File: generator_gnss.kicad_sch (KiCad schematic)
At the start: 0 parts

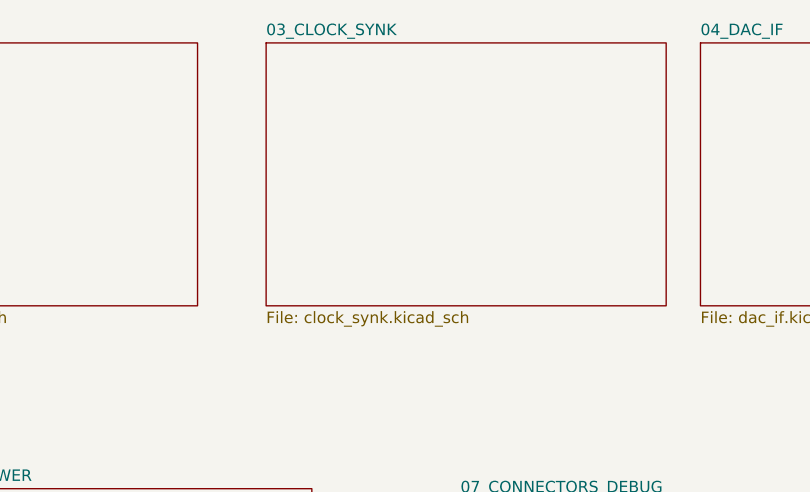
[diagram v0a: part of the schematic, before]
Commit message: Rename schems
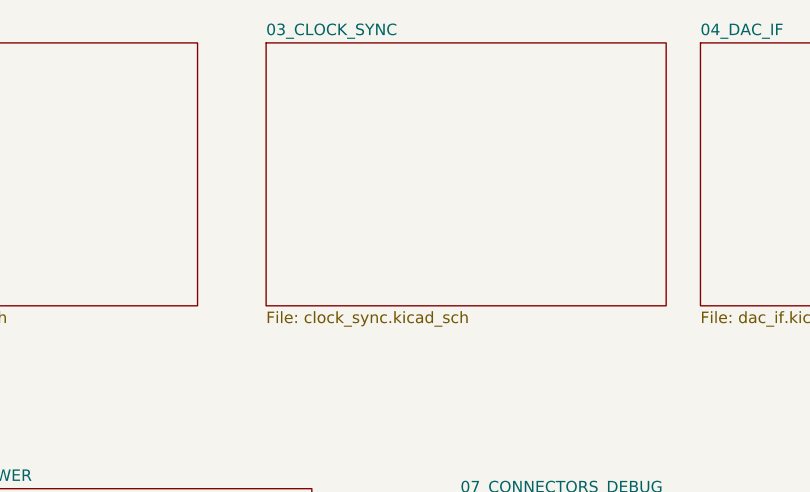
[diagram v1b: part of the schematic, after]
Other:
- sheet 03_CLOCK_SYNK renamed 03_CLOCK_SYNC
- sheet 03_CLOCK_SYNC: file clock_synk.kicad_sch -> clock_sync.kicad_sch
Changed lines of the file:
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@@
 		)
 		(instances
-			(project "immitator_gnns"
+			(project "generator_gnss"
 				(path "/f9f7661c-8604-4706-903b-5ef481cc0e7c"
 					(page "5")
@@
 		)
 		(instances
-			(project "immitator_gnns"
+			(project "generator_gnss"
 				(path "/f9f7661c-8604-4706-903b-5ef481cc0e7c"
 					(page "2")
@@
 		)
 		(instances
-			(project "immitator_gnns"
+			(project "generator_gnss"
 				(path "/f9f7661c-8604-4706-903b-5ef481cc0e7c"
 					(page "8")
@@
 		)
 		(instances
-			(project "immitator_gnns"
+			(project "generator_gnss"
 				(path "/f9f7661c-8604-4706-903b-5ef481cc0e7c"
 					(page "7")
@@
 			(color 0 0 0 0.0000)
 		)
-		(property "Sheetname" "03_CLOCK_SYNK"
+		(property "Sheetname" "03_CLOCK_SYNC"
 			(at 118.11 19.6084 0)
 			(effects
@@
 			)
 		)
-		(property "Sheetfile" "clock_synk.kicad_sch"
+		(property "Sheetfile" "clock_sync.kicad_sch"
 			(at 118.11 50.1146 0)
 			(effects
@@
 		)
 		(instances
-			(project "immitator_gnns"
+			(project "generator_gnss"
 				(path "/f9f7661c-8604-4706-903b-5ef481cc0e7c"
 					(page "4")
@@
 		)
 		(instances
-			(project "immitator_gnns"
+			(project "generator_gnss"
 				(path "/f9f7661c-8604-4706-903b-5ef481cc0e7c"
 					(page "3")
@@
 		)
 		(instances
-			(project "immitator_gnns"
+			(project "generator_gnss"
 				(path "/f9f7661c-8604-4706-903b-5ef481cc0e7c"
 					(page "6")

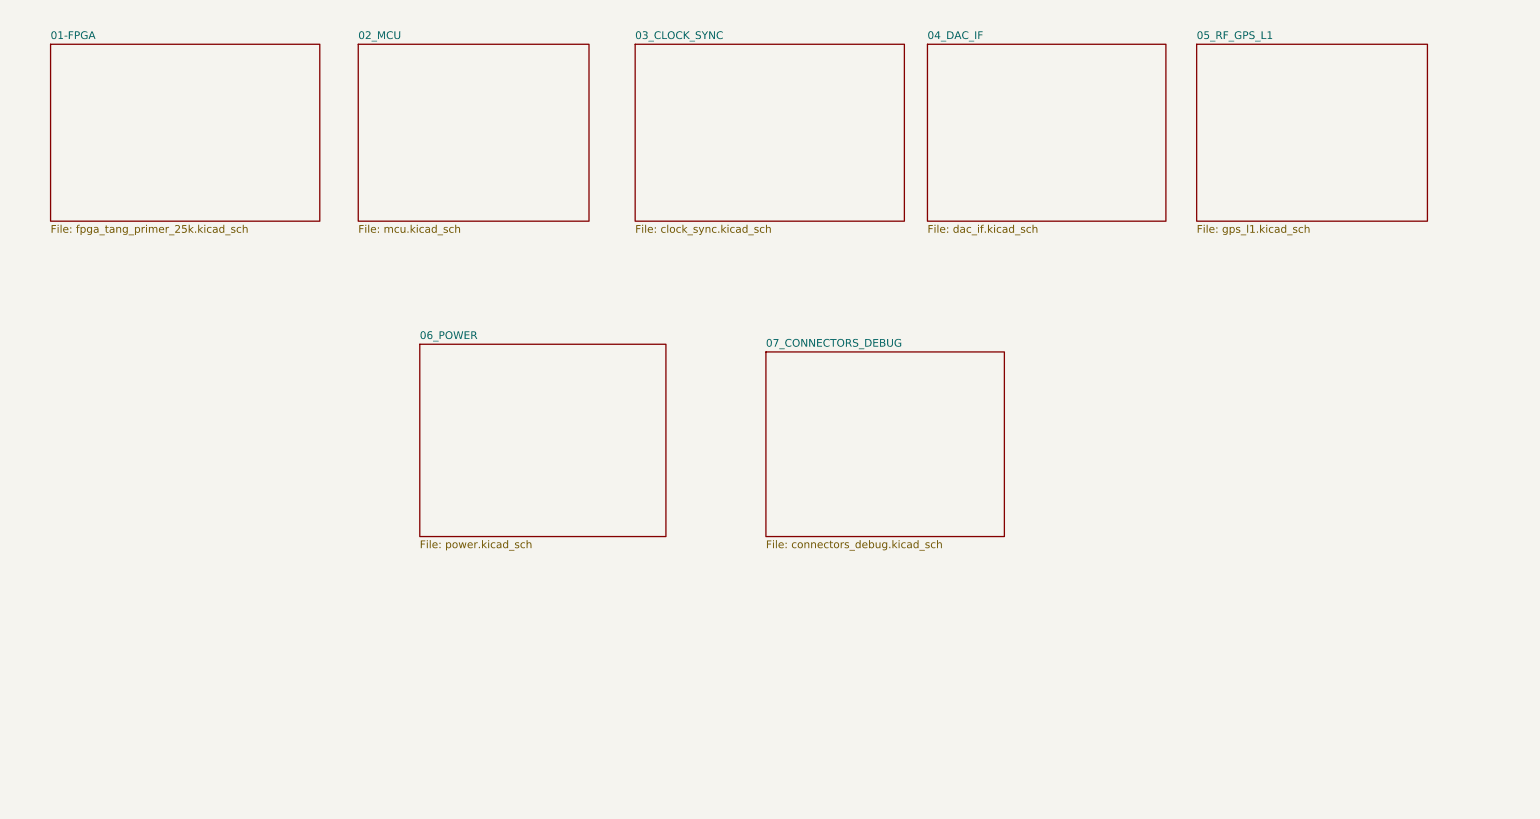
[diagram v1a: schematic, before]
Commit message: Turn to new version Kicad
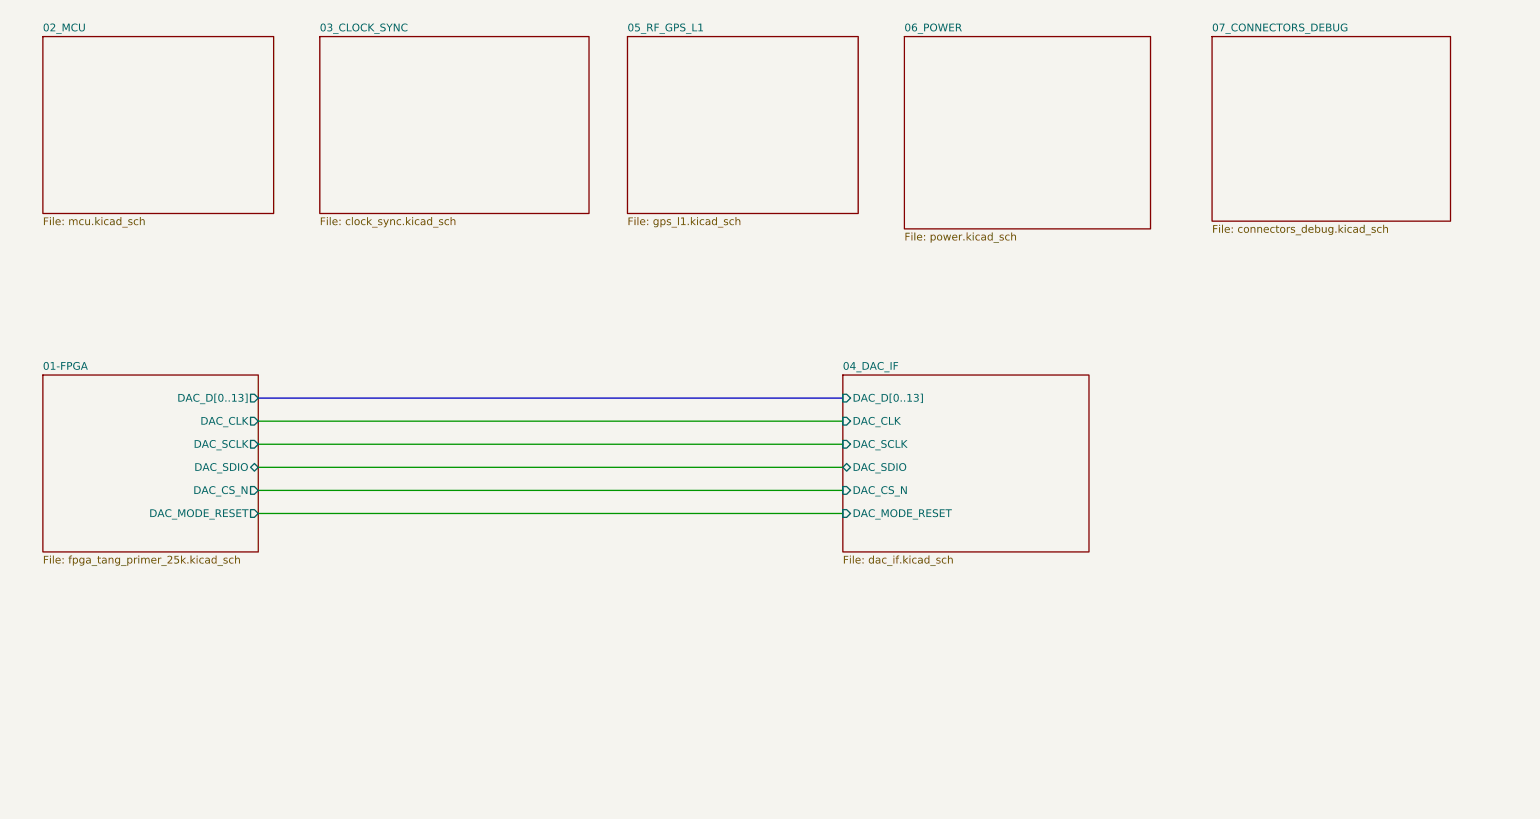
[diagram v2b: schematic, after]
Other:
- sheet 01-FPGA ports: added DAC_CLK, DAC_CS_N, DAC_D[0..13], DAC_MODE_RESET, DAC_SCLK, DAC_SDIO; removed none
- sheet 04_DAC_IF ports: added DAC_CLK, DAC_CS_N, DAC_D[0..13], DAC_MODE_RESET, DAC_SCLK, DAC_SDIO; removed none

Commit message: Make schema of dac and rf partly
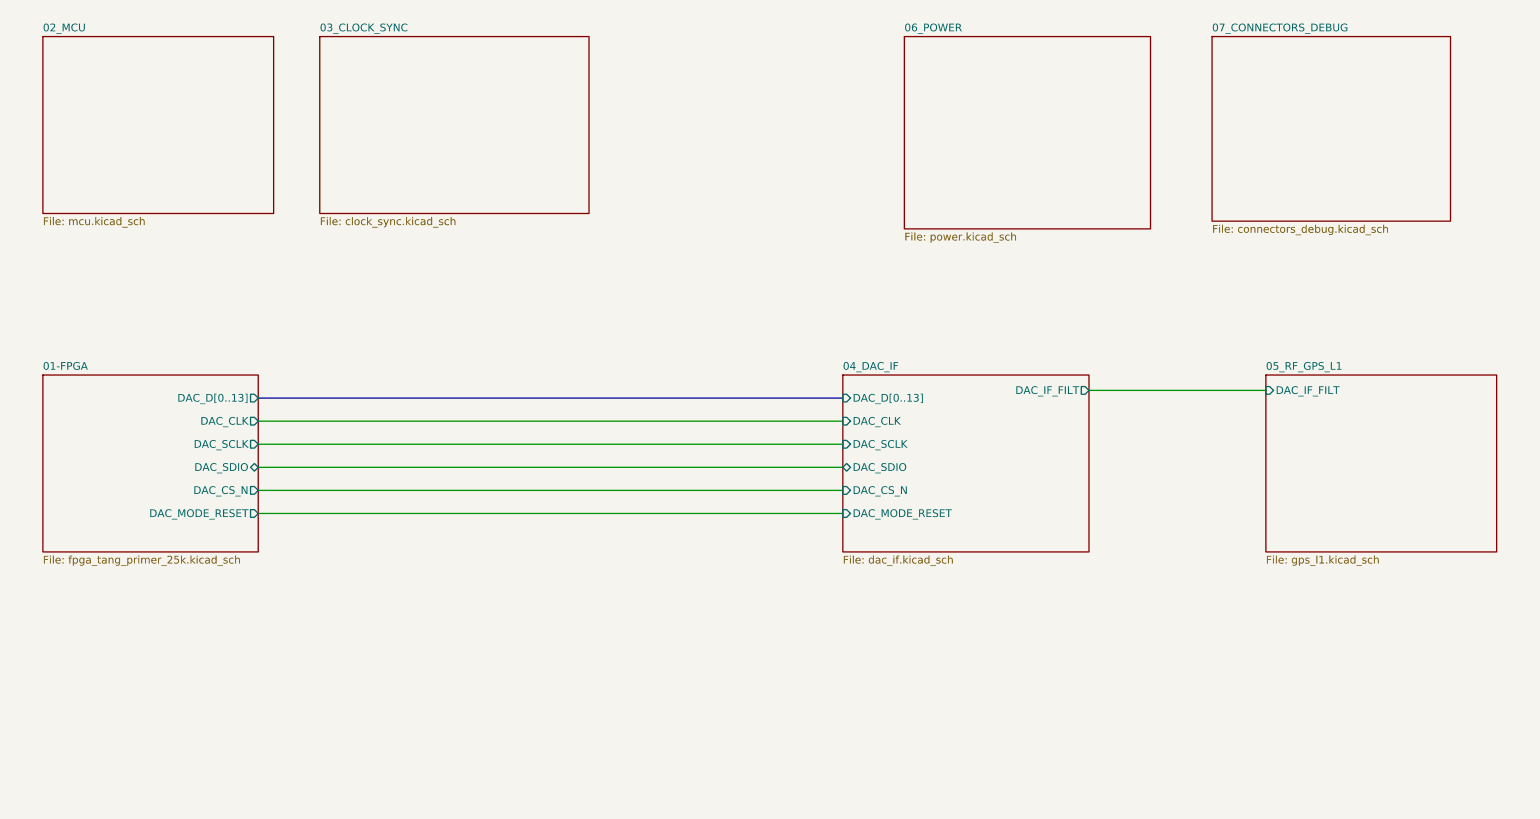
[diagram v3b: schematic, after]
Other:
- sheet 04_DAC_IF ports: added DAC_IF_FILT; removed none
- sheet 05_RF_GPS_L1 ports: added DAC_IF_FILT; removed none
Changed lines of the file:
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@@
+	(wire
+		(pts
+			(xy 193.04 77.47) (xy 222.25 77.47)
+		)
+		(stroke
+			(width 0)
+			(type default)
+		)
+	)
 	(wire
 		(pts
@@
 			)
 		)
+		(pin "DAC_IF_FILT" output
+			(at 193.04 77.47 0)
+			(effects
+				(font
+					(size 1.27 1.27)
+				)
+				(justify right)
+			)
+		)
 		(instances
 			(project "generator_gnss"
@@
 	)
 	(sheet
-		(at 116.84 19.05)
+		(at 222.25 74.93)
 		(size 38.1 29.21)
 		(exclude_from_sim no)
@@
 		)
 		(property "Sheetname" "05_RF_GPS_L1"
-			(at 116.84 18.3384 0)
+			(at 222.25 74.2184 0)
 			(show_name no)
 			(do_not_autoplace no)
@@
 		)
 		(property "Sheetfile" "gps_l1.kicad_sch"
-			(at 116.84 48.8446 0)
-			(show_name no)
-			(do_not_autoplace no)
-			(effects
-				(font
-					(size 1.27 1.27)
-				)
-				(justify left top)
-			)
-		)
+			(at 222.25 104.7246 0)
+			(show_name no)
+			(do_not_autoplace no)
+			(effects
+				(font
+					(size 1.27 1.27)
+				)
+				(justify left top)
+			)
+		)
+		(pin "DAC_IF_FILT" input
+			(at 222.25 77.47 180)
+			(effects
+				(font
+					(size 1.27 1.27)
+				)
+				(justify left)
+			)
+		)

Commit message: checkpoint: integrate GNSS RF and ADF4351 reference clock
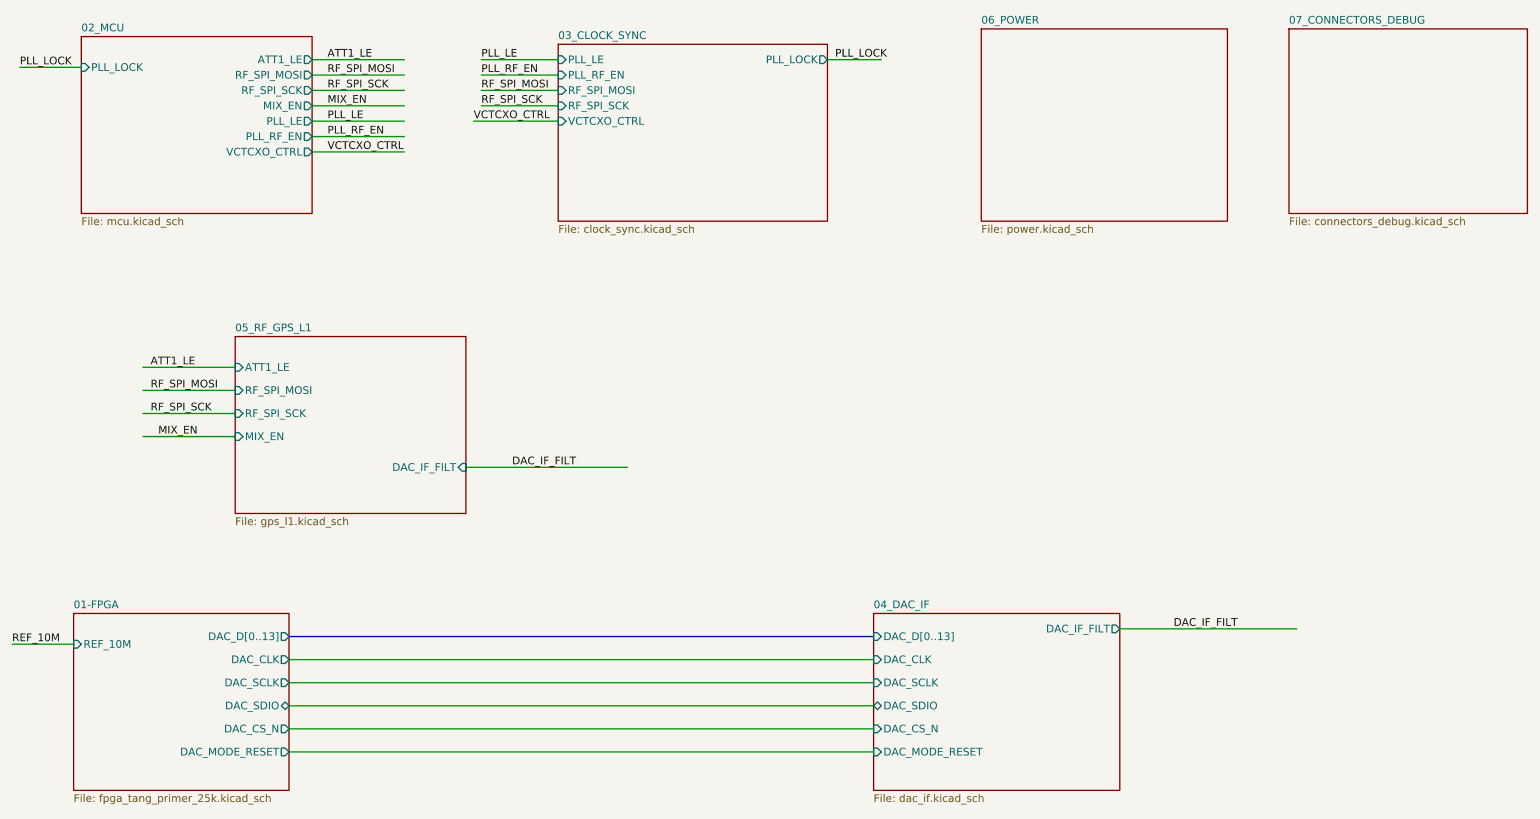
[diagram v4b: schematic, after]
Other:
- sheet 01-FPGA ports: added REF_10M; removed none
- sheet 02_MCU ports: added ATT1_LE, MIX_EN, PLL_LE, PLL_LOCK, PLL_RF_EN, RF_SPI_MOSI, RF_SPI_SCK, VCTCXO_CTRL; removed none
- sheet 03_CLOCK_SYNC ports: added PLL_LE, PLL_LOCK, PLL_RF_EN, RF_SPI_MOSI, RF_SPI_SCK, VCTCXO_CTRL; removed none
- sheet 05_RF_GPS_L1 ports: added ATT1_LE, MIX_EN, RF_SPI_MOSI, RF_SPI_SCK; removed none
